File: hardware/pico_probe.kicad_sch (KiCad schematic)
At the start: 0 parts

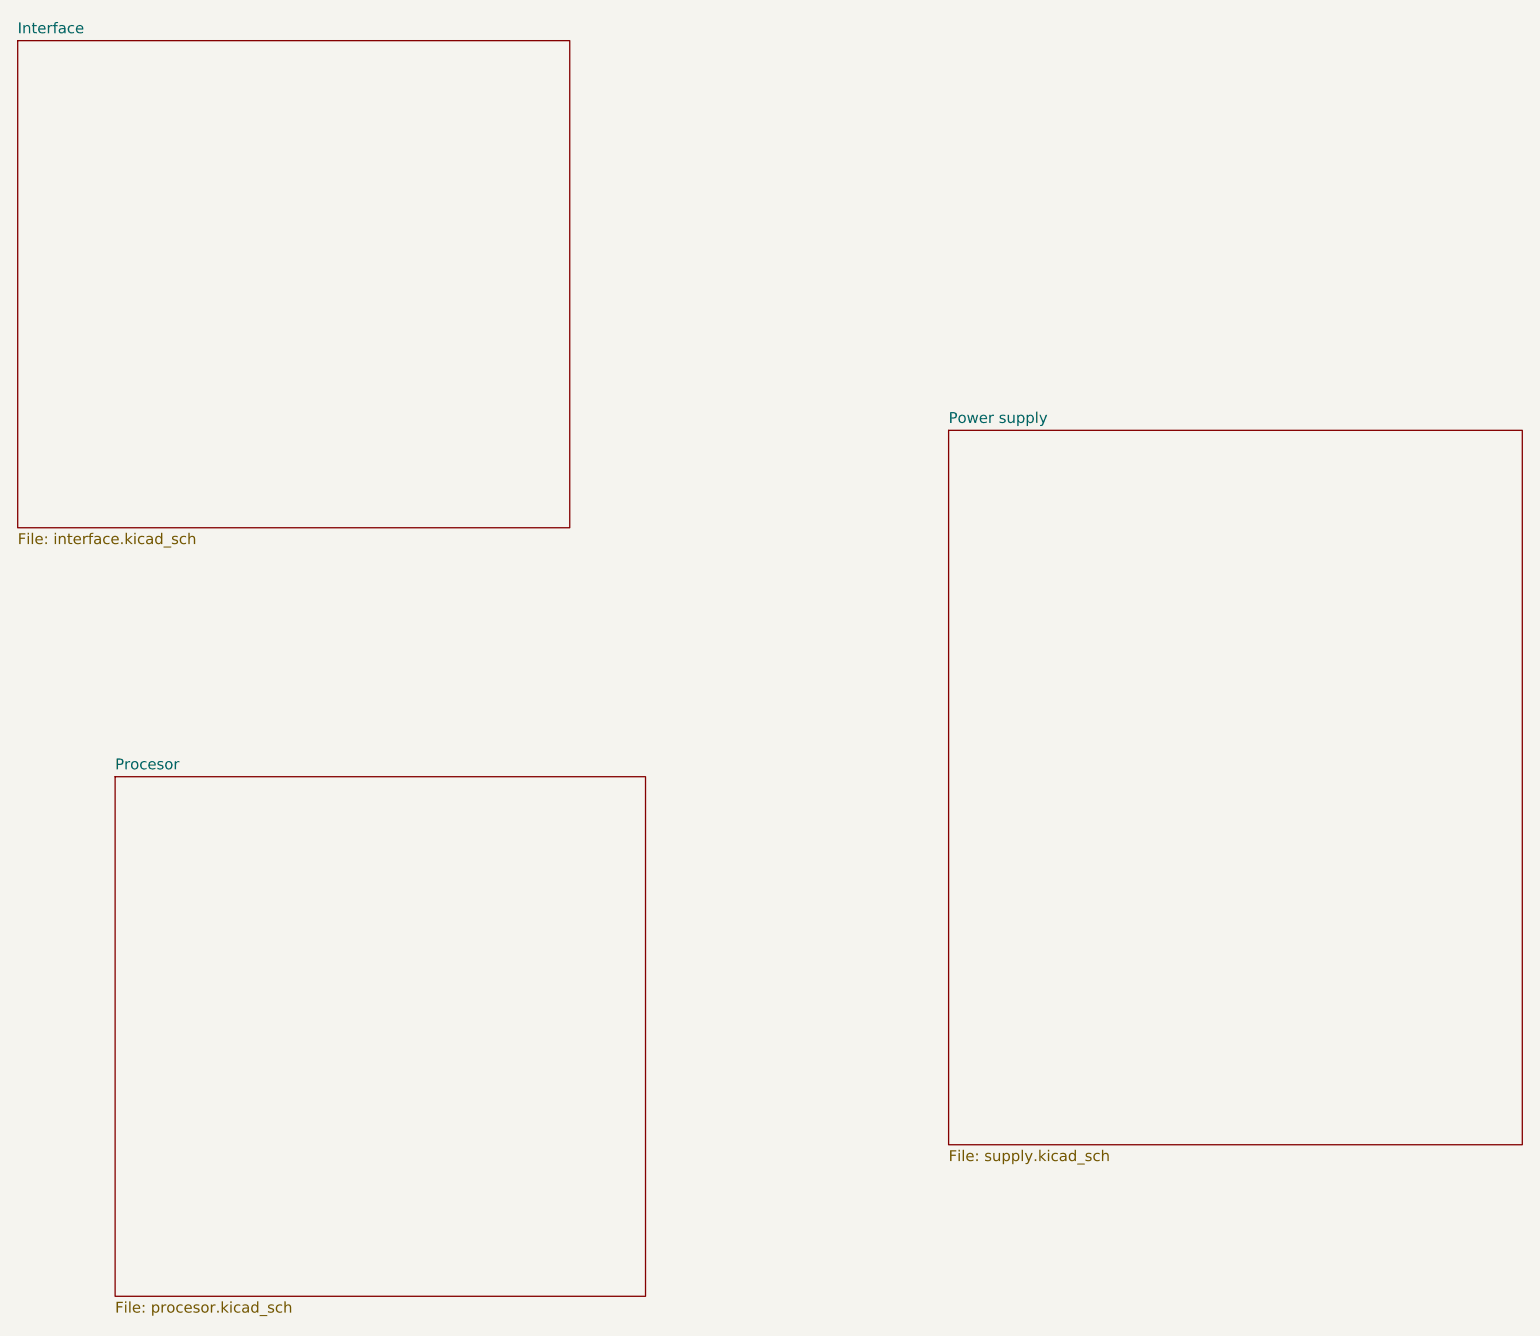
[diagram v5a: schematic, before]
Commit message: hw: Add connection to main sheet
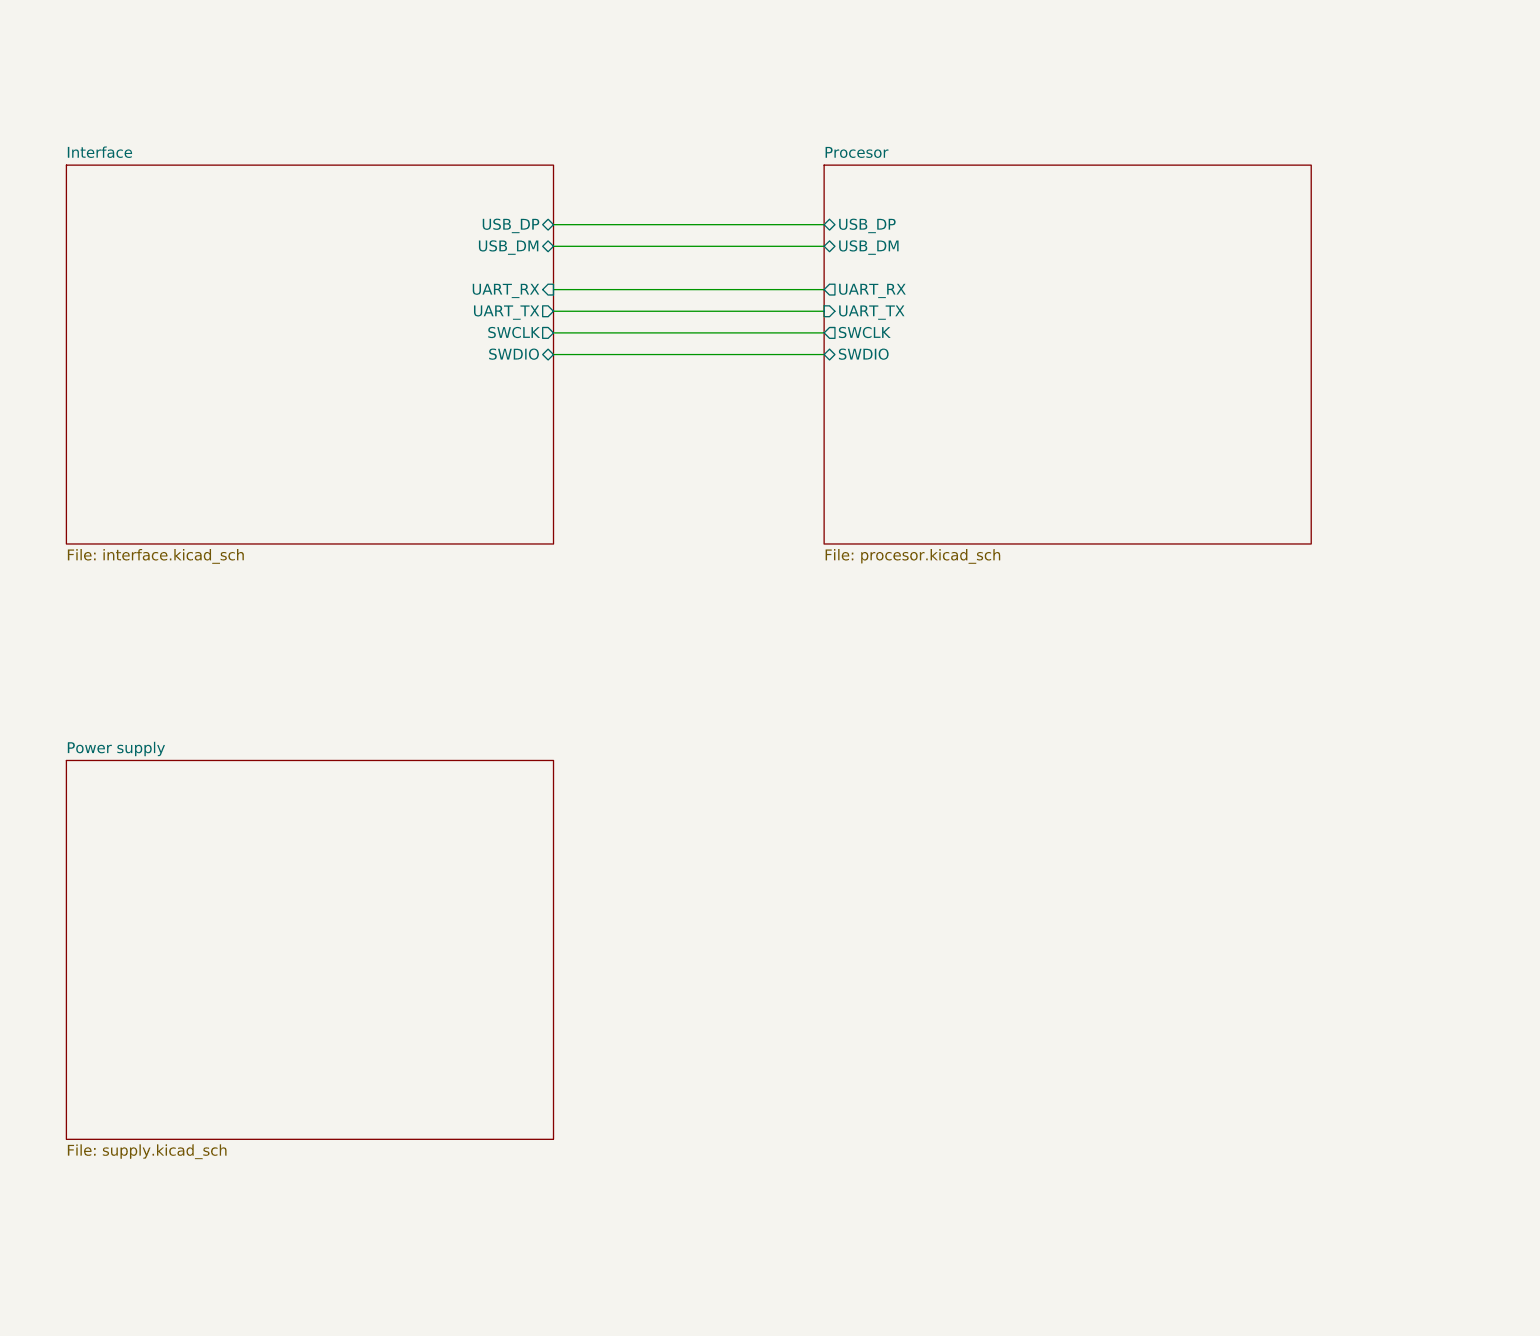
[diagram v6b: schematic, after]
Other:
- sheet Interface ports: added SWCLK, SWDIO, UART_RX, UART_TX, USB_DM, USB_DP; removed none
- sheet Procesor ports: added SWCLK, SWDIO, UART_RX, UART_TX, USB_DM, USB_DP; removed none
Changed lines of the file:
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@@
 (kicad_sch (version 20211123) (generator eeschema)
   (paper "A4")
-  (sheet (at 180.34 77.47) (size 67.31 83.82) (fields_autoplaced)
+  (wire (pts (xy 133.985 68.58) (xy 165.735 68.58))
+    (stroke (width 0) (type default) (color 0 0 0 0))
+  )
+  (wire (pts (xy 133.985 60.96) (xy 165.735 60.96))
+    (stroke (width 0) (type default) (color 0 0 0 0))
+  )
+  (wire (pts (xy 133.985 53.34) (xy 165.735 53.34))
+    (stroke (width 0) (type default) (color 0 0 0 0))
+  )
+  (wire (pts (xy 133.985 63.5) (xy 165.735 63.5))
+    (stroke (width 0) (type default) (color 0 0 0 0))
+  )
+  (wire (pts (xy 133.985 55.88) (xy 165.735 55.88))
+    (stroke (width 0) (type default) (color 0 0 0 0))
+  )
+  (wire (pts (xy 133.985 66.04) (xy 165.735 66.04))
+    (stroke (width 0) (type default) (color 0 0 0 0))
+  )
+  (sheet (at 76.835 116.205) (size 57.15 44.45) (fields_autoplaced)
     (stroke (width 0.1524) (type solid) (color 0 0 0 0))
     (fill (color 0 0 0 0.0000))
-    (property "Sheet name" "Power supply" (id 0) (at 180.34 76.7584 0)
+    (property "Sheet name" "Power supply" (id 0) (at 76.835 115.4934 0)
       (effects (font (size 1.27 1.27)) (justify left bottom))
     )
-    (property "Sheet file" "supply.kicad_sch" (id 1) (at 180.34 161.8746 0)
+    (property "Sheet file" "supply.kicad_sch" (id 1) (at 76.835 161.2396 0)
       (effects (font (size 1.27 1.27)) (justify left top))
     )
   )
-  (sheet (at 82.55 118.11) (size 62.23 60.96) (fields_autoplaced)
+  (sheet (at 165.735 46.355) (size 57.15 44.45) (fields_autoplaced)
     (stroke (width 0.1524) (type solid) (color 0 0 0 0))
     (fill (color 0 0 0 0.0000))
-    (property "Sheet name" "Procesor" (id 0) (at 82.55 117.3984 0)
+    (property "Sheet name" "Procesor" (id 0) (at 165.735 45.6434 0)
       (effects (font (size 1.27 1.27)) (justify left bottom))
     )
-    (property "Sheet file" "procesor.kicad_sch" (id 1) (at 82.55 179.6546 0)
+    (property "Sheet file" "procesor.kicad_sch" (id 1) (at 165.735 91.3896 0)
       (effects (font (size 1.27 1.27)) (justify left top))
     )
+    (pin "UART_TX" input (at 165.735 63.5 180)
+      (effects (font (size 1.27 1.27)) (justify left))
+    )
+    (pin "UART_RX" output (at 165.735 60.96 180)
+      (effects (font (size 1.27 1.27)) (justify left))
+    )
+    (pin "USB_DP" bidirectional (at 165.735 53.34 180)
+      (effects (font (size 1.27 1.27)) (justify left))
+    )
+    (pin "USB_DM" bidirectional (at 165.735 55.88 180)
+      (effects (font (size 1.27 1.27)) (justify left))
+    )
+    (pin "SWCLK" output (at 165.735 66.04 180)
+      (effects (font (size 1.27 1.27)) (justify left))
+    )
+    (pin "SWDIO" bidirectional (at 165.735 68.58 180)
+      (effects (font (size 1.27 1.27)) (justify left))
+    )
   )
-  (sheet (at 71.12 31.75) (size 64.77 57.15) (fields_autoplaced)
+  (sheet (at 76.835 46.355) (size 57.15 44.45) (fields_autoplaced)
     (stroke (width 0.1524) (type solid) (color 0 0 0 0))
     (fill (color 0 0 0 0.0000))
-    (property "Sheet name" "Interface" (id 0) (at 71.12 31.0384 0)
+    (property "Sheet name" "Interface" (id 0) (at 76.835 45.6434 0)
       (effects (font (size 1.27 1.27)) (justify left bottom))
     )
-    (property "Sheet file" "interface.kicad_sch" (id 1) (at 71.12 89.4846 0)
+    (property "Sheet file" "interface.kicad_sch" (id 1) (at 76.835 91.3896 0)
       (effects (font (size 1.27 1.27)) (justify left top))
     )
+    (pin "SWDIO" bidirectional (at 133.985 68.58 0)
+      (effects (font (size 1.27 1.27)) (justify right))
+    )
+    (pin "SWCLK" output (at 133.985 66.04 0)
+      (effects (font (size 1.27 1.27)) (justify right))
+    )
+    (pin "UART_TX" output (at 133.985 63.5 0)
+      (effects (font (size 1.27 1.27)) (justify right))
+    )
+    (pin "UART_RX" input (at 133.985 60.96 0)
+      (effects (font (size 1.27 1.27)) (justify right))
+    )
+    (pin "USB_DM" bidirectional (at 133.985 55.88 0)
+      (effects (font (size 1.27 1.27)) (justify right))
+    )
+    (pin "USB_DP" bidirectional (at 133.985 53.34 0)
+      (effects (font (size 1.27 1.27)) (justify right))
+    )
   )

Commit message: hw: Add the title block informations
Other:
- company: (none) -> Jan Krejčí
- title: (none) -> Pico probe
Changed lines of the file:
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@@
 (kicad_sch (version 20211123) (generator eeschema)
   (paper "A4")
+  (title_block
+    (title "Pico probe")
+    (date "2022-04-03")
+    (rev "22.04")
+    (company "Jan Krejčí")
+  )
   (wire (pts (xy 133.985 68.58) (xy 165.735 68.58))
     (stroke (width 0) (type default) (color 0 0 0 0))
